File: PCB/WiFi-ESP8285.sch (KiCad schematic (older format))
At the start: 24 parts, among them SW2 B3U-1000P, T1 1909763-1, U4 ESP8285, X3 FA-128_26.0000MF10Z-AC3

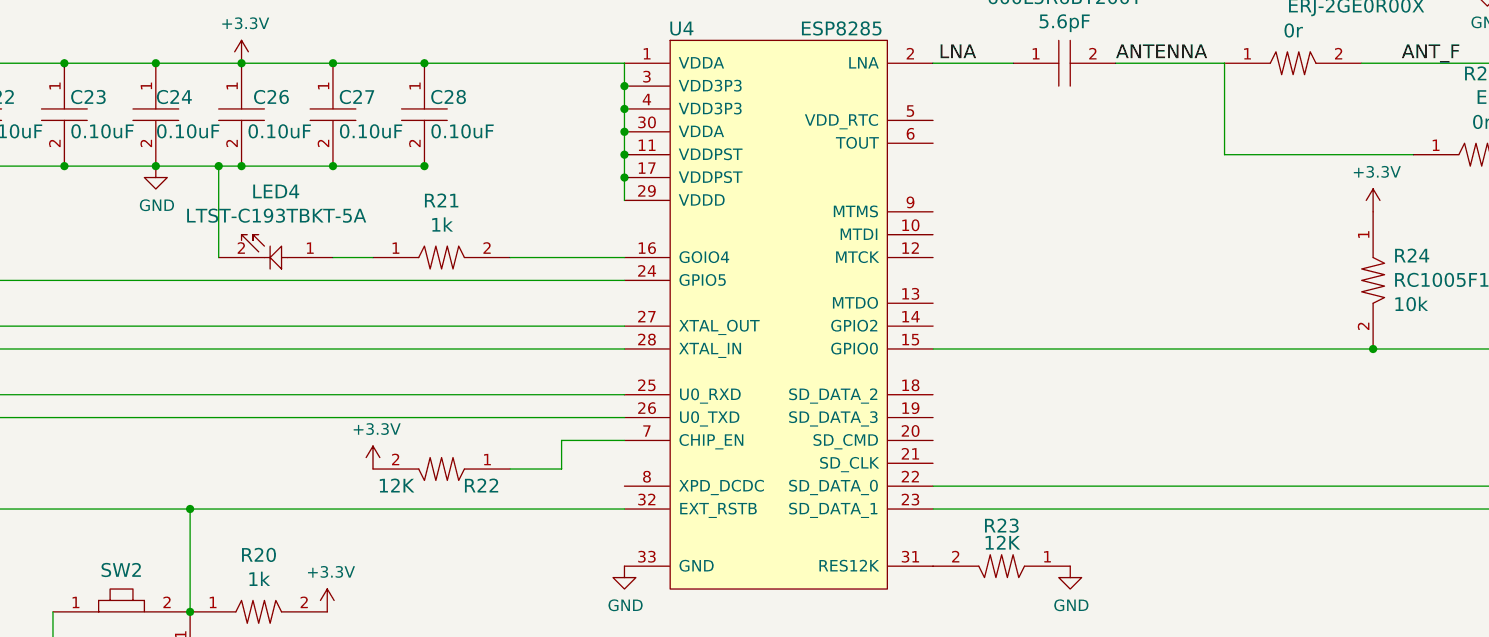
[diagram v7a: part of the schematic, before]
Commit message: ESP Footprint Error and RF improvement
ESP8285 footprint was wrong, made when I was still learning kiCAD.
Footprint change and entire topology reconstructed and rerouted. Added
ground pours and heavy via stitching to improve RF performance. Also
started an ESP-12E module based variant. Both will be fabbed at the same
time.
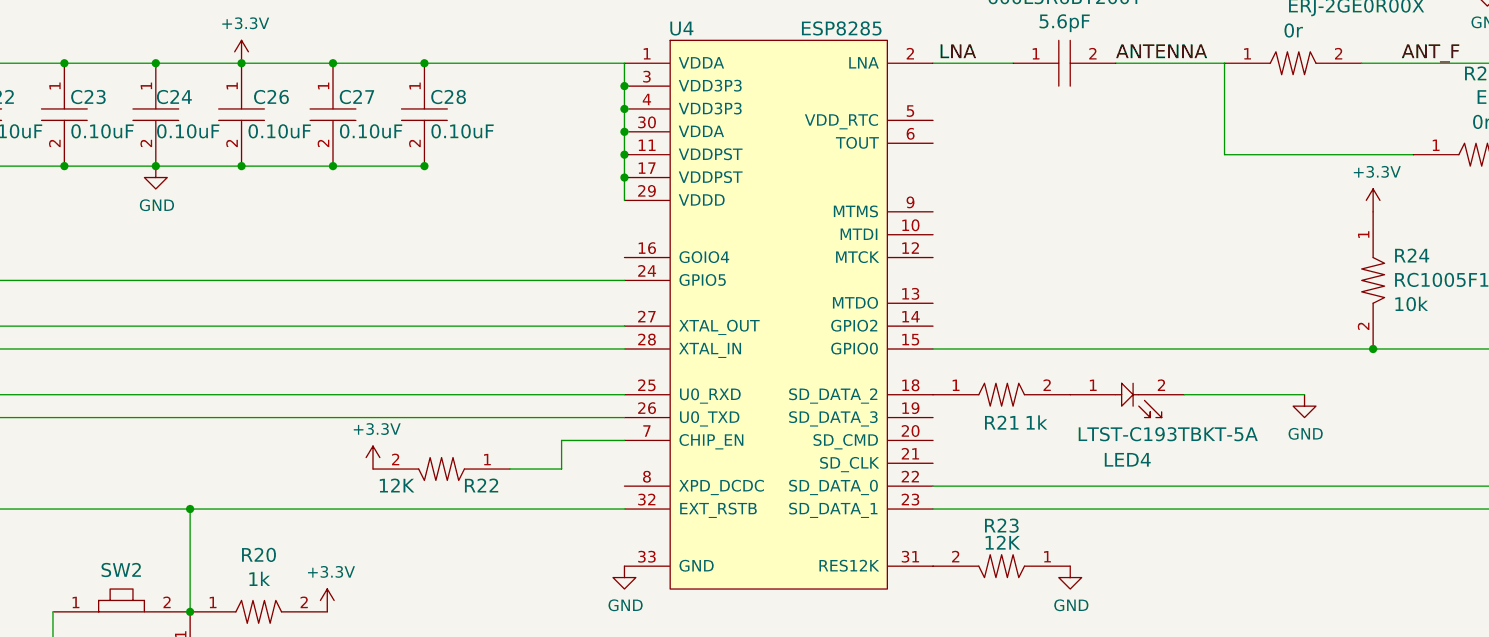
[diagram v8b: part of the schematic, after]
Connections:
- net at LED4.1: now also R21.2; no longer R21.1
- net at U4.16 (GOIO4): no longer R21.2
- net at U4.18 (SD_DATA_2): now also R21.1
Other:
- moved on the sheet: LED4, R21
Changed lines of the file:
@@
 L LTST-C193TBKT-5A LED4
 U 1 1 57EACEB9
-P 3875 3250
-F 0 "LED4" H 3875 2963 60  0000 C CNN
-F 1 "LTST-C193TBKT-5A" H 3875 3069 60  0000 C CNN
-F 2 "PCB_Footprints:LED0603" H 5300 5175 60  0001 C CNN
-F 3 "http://optoelectronics.liteon.com/upload/download/DS22-2004-060/P_100_LTST-C193TBKT-5A.pdf" H 5500 5300 60  0001 C CNN
-F 4 "0.06102 @ 6000" H 3725 3450 60  0001 C CNN "Cost"
-F 5 "8 Sept 2016" H 3825 3550 60  0001 C CNN "Date Created"
-F 6 "8 Sept 2016" H 3925 3650 60  0001 C CNN "Date Modified"
-F 7 "Adam Vadala-Roth" H 4025 3750 60  0001 C CNN "Designer"
-F 8 "0.55mm" H 4125 3850 60  0001 C CNN "Height"
-F 9 "Yes" H 4225 3950 60  0001 C CNN "RhoS?"
-F 10 "Lite-On Inc" H 4325 4050 60  0001 C CNN "MFR"
-F 11 "LTST-C193TBKT-5A" H 4425 4150 60  0001 C CNN "MFR#"
-F 12 "SMT/SMD" H 4525 4250 60  0001 C CNN "Mounting"
-F 13 "2" H 4625 4350 60  0001 C CNN "Pin Count#"
-F 14 "Active" H 4725 4450 60  0001 C CNN "Status"
-F 15 "N/A" H 4825 4550 60  0001 C CNN "Tolerance"
-F 16 "0603 LED" H 4925 4650 60  0001 C CNN "Type"
-F 17 "2.8V Forward Voltage" H 5025 4750 60  0001 C CNN "Voltage"
-F 18 "N/A" H 5125 4850 60  0001 C CNN "Wattage"
-F 19 "N/A" H 5225 4950 60  0001 C CNN "Component-Value"
-F 20 "Blue 470nm LED Indication - Discrete 2.8V 0603 (1608 Metric)" H 5325 5050 60  0001 C CNN "Description"
-	1    3875 3250
-	-1   0    0    1
+P 7600 3850
+F 0 "LED4" H 7600 3563 60  0000 C CNN
+F 1 "LTST-C193TBKT-5A" H 7775 3675 60  0000 C CNN
+F 2 "PCB_Footprints:LED0603" H 9025 5775 60  0001 C CNN
+F 3 "http://optoelectronics.liteon.com/upload/download/DS22-2004-060/P_100_LTST-C193TBKT-5A.pdf" H 9225 5900 60  0001 C CNN
+F 4 "0.06102 @ 6000" H 7450 4050 60  0001 C CNN "Cost"
+F 5 "8 Sept 2016" H 7550 4150 60  0001 C CNN "Date Created"
+F 6 "8 Sept 2016" H 7650 4250 60  0001 C CNN "Date Modified"
+F 7 "Adam Vadala-Roth" H 7750 4350 60  0001 C CNN "Designer"
+F 8 "0.55mm" H 7850 4450 60  0001 C CNN "Height"
+F 9 "Yes" H 7950 4550 60  0001 C CNN "RhoS?"
+F 10 "Lite-On Inc" H 8050 4650 60  0001 C CNN "MFR"
+F 11 "LTST-C193TBKT-5A" H 8150 4750 60  0001 C CNN "MFR#"
+F 12 "SMT/SMD" H 8250 4850 60  0001 C CNN "Mounting"
+F 13 "2" H 8350 4950 60  0001 C CNN "Pin Count#"
+F 14 "Active" H 8450 5050 60  0001 C CNN "Status"
+F 15 "N/A" H 8550 5150 60  0001 C CNN "Tolerance"
+F 16 "0603 LED" H 8650 5250 60  0001 C CNN "Type"
+F 17 "2.8V Forward Voltage" H 8750 5350 60  0001 C CNN "Voltage"
+F 18 "N/A" H 8850 5450 60  0001 C CNN "Wattage"
+F 19 "N/A" H 8950 5550 60  0001 C CNN "Component-Value"
+F 20 "Blue 470nm LED Indication - Discrete 2.8V 0603 (1608 Metric)" H 9050 5650 60  0001 C CNN "Description"
+	1    7600 3850
+	1    0    0    -1
 $EndComp
 $Comp
 L RC1005F102CS R21
 U 1 1 57EAD2D3
-P 4600 3250
-F 0 "R21" H 4600 3497 60  0000 C CNN
-F 1 "RC1005F102CS" H 4600 3497 60  0001 C CNN
-F 2 "PCB_Footprints:R0402" H 4200 3500 60  0001 C CNN
-F 3 "https://media.digikey.com/pdf/Data%20Sheets/Samsung%20PDFs/RC_Series_ds.pdf" H 4300 3700 60  0001 C CNN
-F 4 "0.00173 @ 5000" H 6150 5200 60  0001 C CNN "Cost"
-F 5 "5 Sept 2016" H 4500 3800 60  0001 C CNN "Date Created"
-F 6 "5 Sept 2016" H 4600 3900 60  0001 C CNN "Date Modified"
-F 7 "Adam Vadala-Roth" H 4700 4000 60  0001 C CNN "Designer"
-F 8 "0.4mm" H 4800 4100 60  0001 C CNN "Height"
-F 9 "Yes" H 4900 4200 60  0001 C CNN "RHoS?"
-F 10 "Samsung Electro-Mechanics America, Inc." H 5000 4300 60  0001 C CNN "MFR"
-F 11 "RC1005F102CS" H 5100 4400 60  0001 C CNN "MFR#"
-F 12 "SMT/SMD" H 5200 4500 60  0001 C CNN "Mounting"
-F 13 "2" H 5300 4600 60  0001 C CNN "Pin Count#"
-F 14 "Active" H 5400 4700 60  0001 C CNN "Status"
-F 15 "%" H 5500 4800 60  0001 C CNN "Tolerance"
-F 16 "passive" H 5600 4900 60  0001 C CNN "Type"
-F 17 "N/A" H 5700 5000 60  0001 C CNN "Voltage"
-F 18 "1/16" H 5800 5100 60  0001 C CNN "Wattage"
-F 19 "1k" H 4600 3391 60  0000 C CNN "Component-Value"
-F 20 "RES SMD 1K OHM 1% 1/16W 0402" H 6000 5300 60  0001 C CNN "Description"
-	1    4600 3250
+P 7050 3850
+F 0 "R21" H 7050 3725 60  0000 C CNN
+F 1 "RC1005F102CS" H 7050 4097 60  0001 C CNN
+F 2 "PCB_Footprints:R0402" H 6650 4100 60  0001 C CNN
+F 3 "https://media.digikey.com/pdf/Data%20Sheets/Samsung%20PDFs/RC_Series_ds.pdf" H 6750 4300 60  0001 C CNN
+F 4 "0.00173 @ 5000" H 8600 5800 60  0001 C CNN "Cost"
+F 5 "5 Sept 2016" H 6950 4400 60  0001 C CNN "Date Created"
+F 6 "5 Sept 2016" H 7050 4500 60  0001 C CNN "Date Modified"
+F 7 "Adam Vadala-Roth" H 7150 4600 60  0001 C CNN "Designer"
+F 8 "0.4mm" H 7250 4700 60  0001 C CNN "Height"
+F 9 "Yes" H 7350 4800 60  0001 C CNN "RHoS?"
+F 10 "Samsung Electro-Mechanics America, Inc." H 7450 4900 60  0001 C CNN "MFR"
+F 11 "RC1005F102CS" H 7550 5000 60  0001 C CNN "MFR#"
+F 12 "SMT/SMD" H 7650 5100 60  0001 C CNN "Mounting"
+F 13 "2" H 7750 5200 60  0001 C CNN "Pin Count#"
+F 14 "Active" H 7850 5300 60  0001 C CNN "Status"
+F 15 "%" H 7950 5400 60  0001 C CNN "Tolerance"
+F 16 "passive" H 8050 5500 60  0001 C CNN "Type"
+F 17 "N/A" H 8150 5600 60  0001 C CNN "Voltage"
+F 18 "1/16" H 8250 5700 60  0001 C CNN "Wattage"
+F 19 "1k" H 7200 3725 60  0000 C CNN "Component-Value"
+F 20 "RES SMD 1K OHM 1% 1/16W 0402" H 8450 5900 60  0001 C CNN "Description"
+	1    7050 3850
 	1    0    0    -1
 $EndComp
@@
 Connection ~ 2900 5250
 Wire Wire Line
-	5400 3250 4900 3250
-Wire Wire Line
-	4125 3250 4300 3250
-Wire Wire Line
-	3625 3250 3625 2850
-Connection ~ 3625 2850
-Wire Wire Line
 	1625 5325 2375 5325
 Wire Wire Line
@@
 Text Label 6775 2400 0    60   ~ 0
 LNA
+$Comp
+L GND #PWR?
+U 1 1 5803F0C5
+P 8375 3850
+F 0 "#PWR?" H 8375 3600 50  0001 C CNN
+F 1 "GND" H 8380 3677 50  0000 C CNN
+F 2 "" H 8375 3850 50  0000 C CNN
+F 3 "" H 8375 3850 50  0000 C CNN
+	1    8375 3850
+	1    0    0    -1
+$EndComp
+Wire Wire Line
+	8375 3850 7850 3850
 $EndSCHEMATC
